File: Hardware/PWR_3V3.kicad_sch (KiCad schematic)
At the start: 11 parts, among them U19 SP3485EN

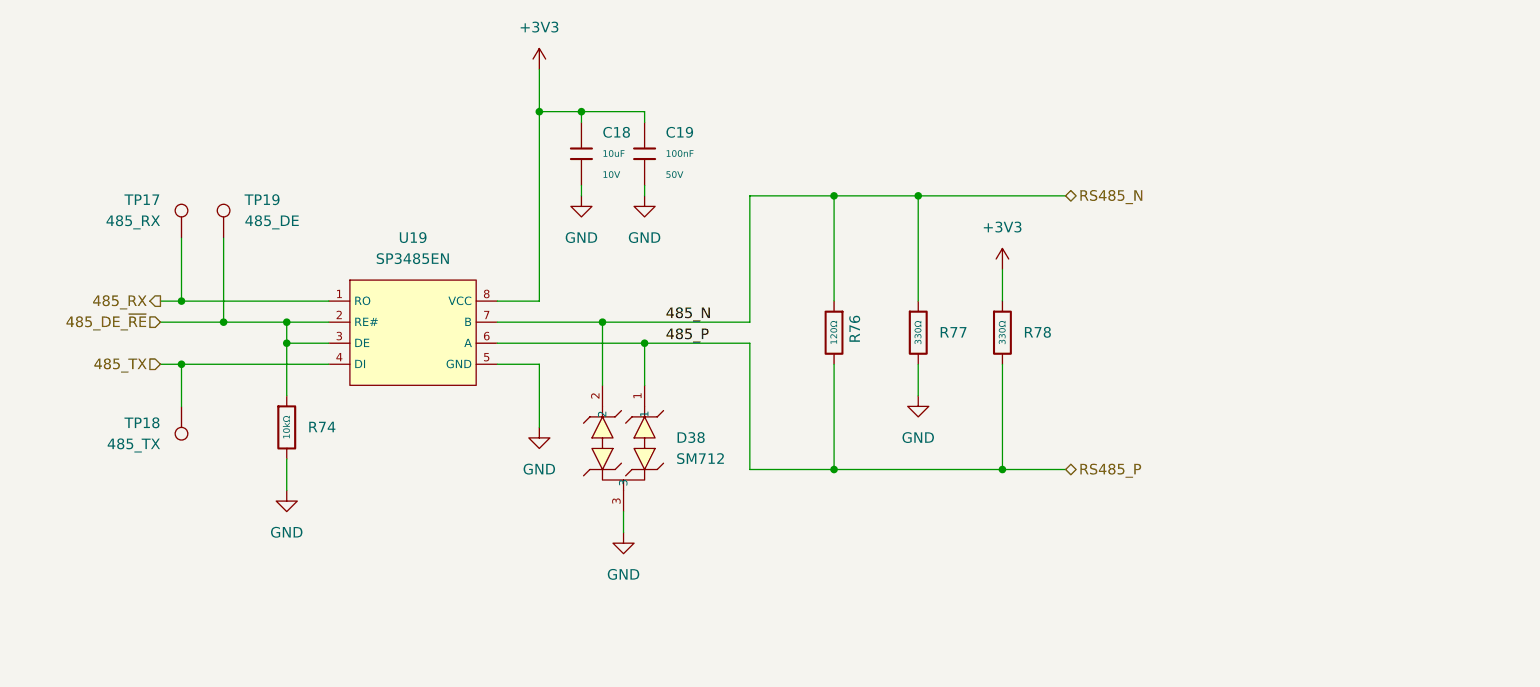
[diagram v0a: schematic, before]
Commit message: remove unused sheets
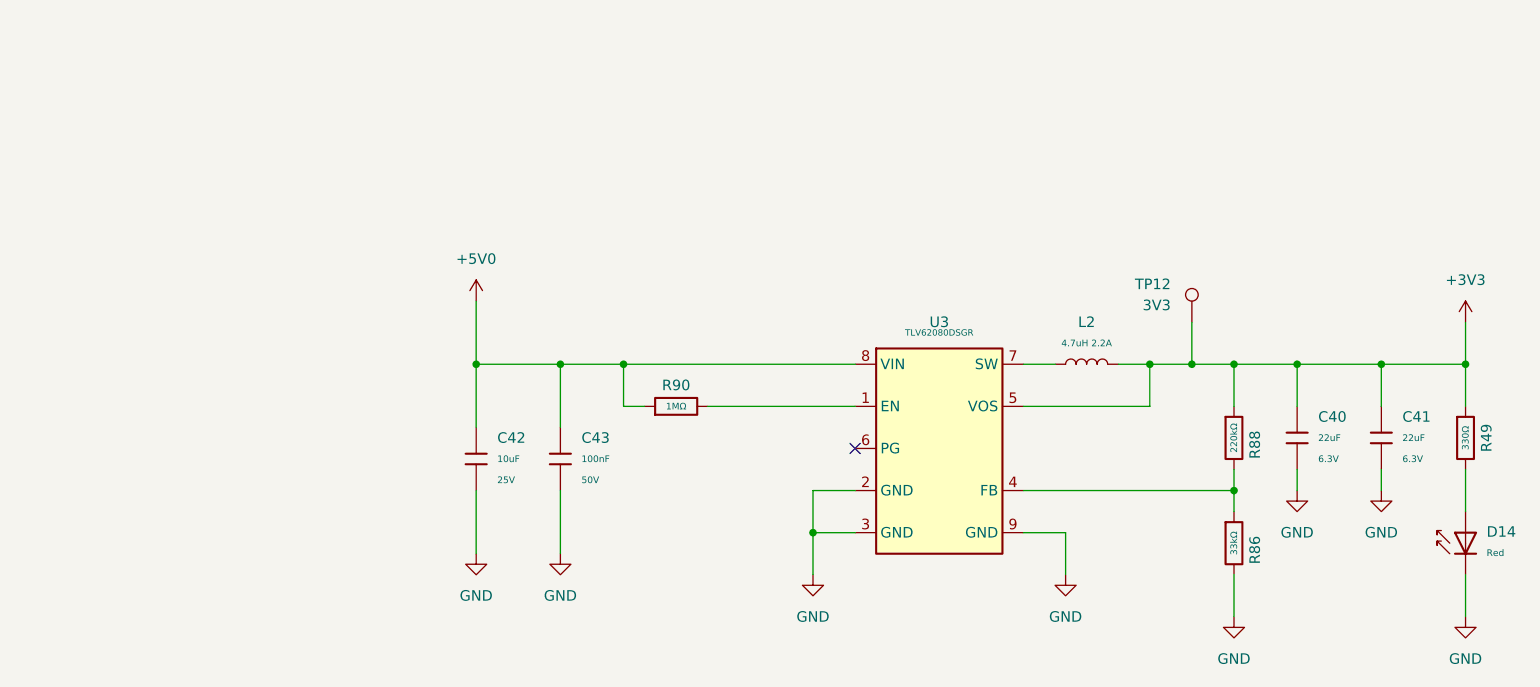
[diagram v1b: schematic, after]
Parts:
- removed C18: 10uF, PCM_JLCPCB:C_0603, symbol PCM_JLCPCB-Capacitors:0603,10uF
- removed C19: 100nF, PCM_JLCPCB:C_0603, symbol PCM_JLCPCB-Capacitors:0603,100nF
- removed D38: SM712, PCM_JLCPCB:SOT-23-3_L2.9-W1.3-P1.90-LS2.4-BR, symbol PCM_JLCPCB-Diode-Packages:TVS-Bi, SM712
- removed R74: 10kΩ, PCM_JLCPCB:R_0603, symbol PCM_JLCPCB-Resistors:0603,10kΩ
- removed R76: 120Ω, PCM_JLCPCB:R_0805, symbol PCM_JLCPCB-Resistors:0805,120Ω
- removed R77, R78: 330Ω, PCM_JLCPCB:R_0603, symbol PCM_JLCPCB-Resistors:0603,330Ω
- removed TP17: 485_RX, TestPoint:TestPoint_Pad_D1.0mm, symbol Connector:TestPoint
- removed TP18: 485_TX, TestPoint:TestPoint_Pad_D1.0mm, symbol Connector:TestPoint
- removed TP19: 485_DE, TestPoint:TestPoint_Pad_D1.0mm, symbol Connector:TestPoint
- removed U19: SP3485EN, PCM_JLCPCB:SOIC-8_L5.0-W4.0-P1.27-LS6.0-BL, symbol PCM_JLCPCB-Interface:Transceiver, RS485/422, 10Mbps, SP3485EN-L/TR
- added C40, C41: 22uF, PCM_JLCPCB:C_0603, symbol PCM_JLCPCB-Capacitors:0603,22uF
- added C42: 10uF, PCM_JLCPCB:C_0603, symbol PCM_JLCPCB-Capacitors:0603,10uF,(2)
- added C43: 100nF, PCM_JLCPCB:C_0603, symbol PCM_JLCPCB-Capacitors:0603,100nF
- added D14: Red, PCM_JLCPCB:D_0603, symbol PCM_JLCPCB-Diodes:LED,0603,Red
- added L2: 4.7uH 2.2A, EASYEDA2KICAD:L1008, symbol PCM_JLCPCB-Extended:IND, 1uH 2A
- added R49: 330Ω, PCM_JLCPCB:R_0603, symbol PCM_JLCPCB-Resistors:0603,330Ω
- added R86: 33kΩ, PCM_JLCPCB:R_0603, symbol PCM_JLCPCB-Resistors:0603,33kΩ
- added R88: 220kΩ, PCM_JLCPCB:R_0603, symbol PCM_JLCPCB-Resistors:0603,220kΩ
- added R90: 1MΩ, PCM_JLCPCB:R_0603, symbol PCM_JLCPCB-Resistors:0603,1MΩ
- added TP12: 3V3, TestPoint:TestPoint_Pad_D1.0mm, symbol Connector:TestPoint
- added U3: TLV62080DSGR, Package_SON:WSON-8-1EP_2x2mm_P0.5mm_EP0.9x1.6mm, symbol PCM_JLCPCB-Extended:PMIC, TLV62080DSGR
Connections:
- net +3V3: now also C40.1, C41.1, L2.2, R49.1, R88.1, TP12.1, U3.5 (VOS)
- net GND: now also C40.2, C41.2, C42.2, C43.2, D14.1, R86.2, U3.2 (GND), U3.3 (GND), U3.9 (GND)
- new net: D14.2, R49.2
- new net: R90.2, U3.1 (EN)
- new net: R86.1, R88.2, U3.4 (FB)
- new net: L2.1, U3.7 (SW)
- new net +5V0: C42.1, C43.1, R90.1, U3.8 (VIN)
- no-connect marks 0 -> 1
